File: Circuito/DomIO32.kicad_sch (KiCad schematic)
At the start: 69 parts, among them J1 Conector 1x5, J2 Bornera x2, J3 Bornera x3, J4 Bornera x3, J5 Conn_01x04, J6 Bornera x3, J7 Bornera x2, K1 FINDER-36.11, K2 FINDER-36.11, K3 FINDER-36.11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

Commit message: Componentes actualizados
Regulador 3v3 que soporta Vin de 18V
ESP-02 Version nueva
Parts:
- U1: value LM1117-3.3 -> (none); footprint Package_TO_SOT_SMD:SOT-223-3_TabPin2 -> (none)
- U3: value ESP-02 -> (none); footprint RF_Module:ESP-WROOM-02 -> (none)
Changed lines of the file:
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@@
     (in_bom yes) (on_board yes)
     (property "Reference" "U3" (id 0) (at 180.34 17.3482 0))
-    (property "Value" "ESP-02" (id 1) (at 180.34 19.6596 0))
-    (property "Footprint" "RF_Module:ESP-WROOM-02" (id 2) (at 171.45 50.8 0)
+    (property "Value" "" (id 1) (at 180.34 19.6596 0))
+    (property "Footprint" "" (id 2) (at 171.45 50.8 0)
       (effects (font (size 1.27 1.27) italic) hide)
     )
@@
     (in_bom yes) (on_board yes)
     (property "Reference" "U1" (id 0) (at 77.47 24.3332 0))
-    (property "Value" "LM1117-3.3" (id 1) (at 77.47 26.6446 0))
-    (property "Footprint" "Package_TO_SOT_SMD:SOT-223-3_TabPin2" (id 2) (at 77.47 30.48 0)
+    (property "Value" "" (id 1) (at 77.47 26.6446 0))
+    (property "Footprint" "" (id 2) (at 77.47 30.48 0)
       (effects (font (size 1.27 1.27)) hide)
     )
@@
     )
     (path "/00000000-0000-0000-0000-00005e867b53"
-      (reference "U1") (unit 1) (value "LM1117-3.3") (footprint "Package_TO_SOT_SMD:SOT-223-3_TabPin2")
+      (reference "U1") (unit 1) (value "ZLDO1117QG33TADICT-ND") (footprint "Package_TO_SOT_SMD:SOT-223-3_TabPin2")
     )
     (path "/00000000-0000-0000-0000-0000622ef159"
@@
     )
     (path "/00000000-0000-0000-0000-00005dcb6f71"
-      (reference "U3") (unit 1) (value "ESP-02") (footprint "RF_Module:ESP-WROOM-02")
-    )
-  )
+      (reference "U3") (unit 1) (value "1965-ESP-WROOM-02D-N4CT-ND") (footprint "RF_Module:ESP-WROOM-02")
+    )
+  )

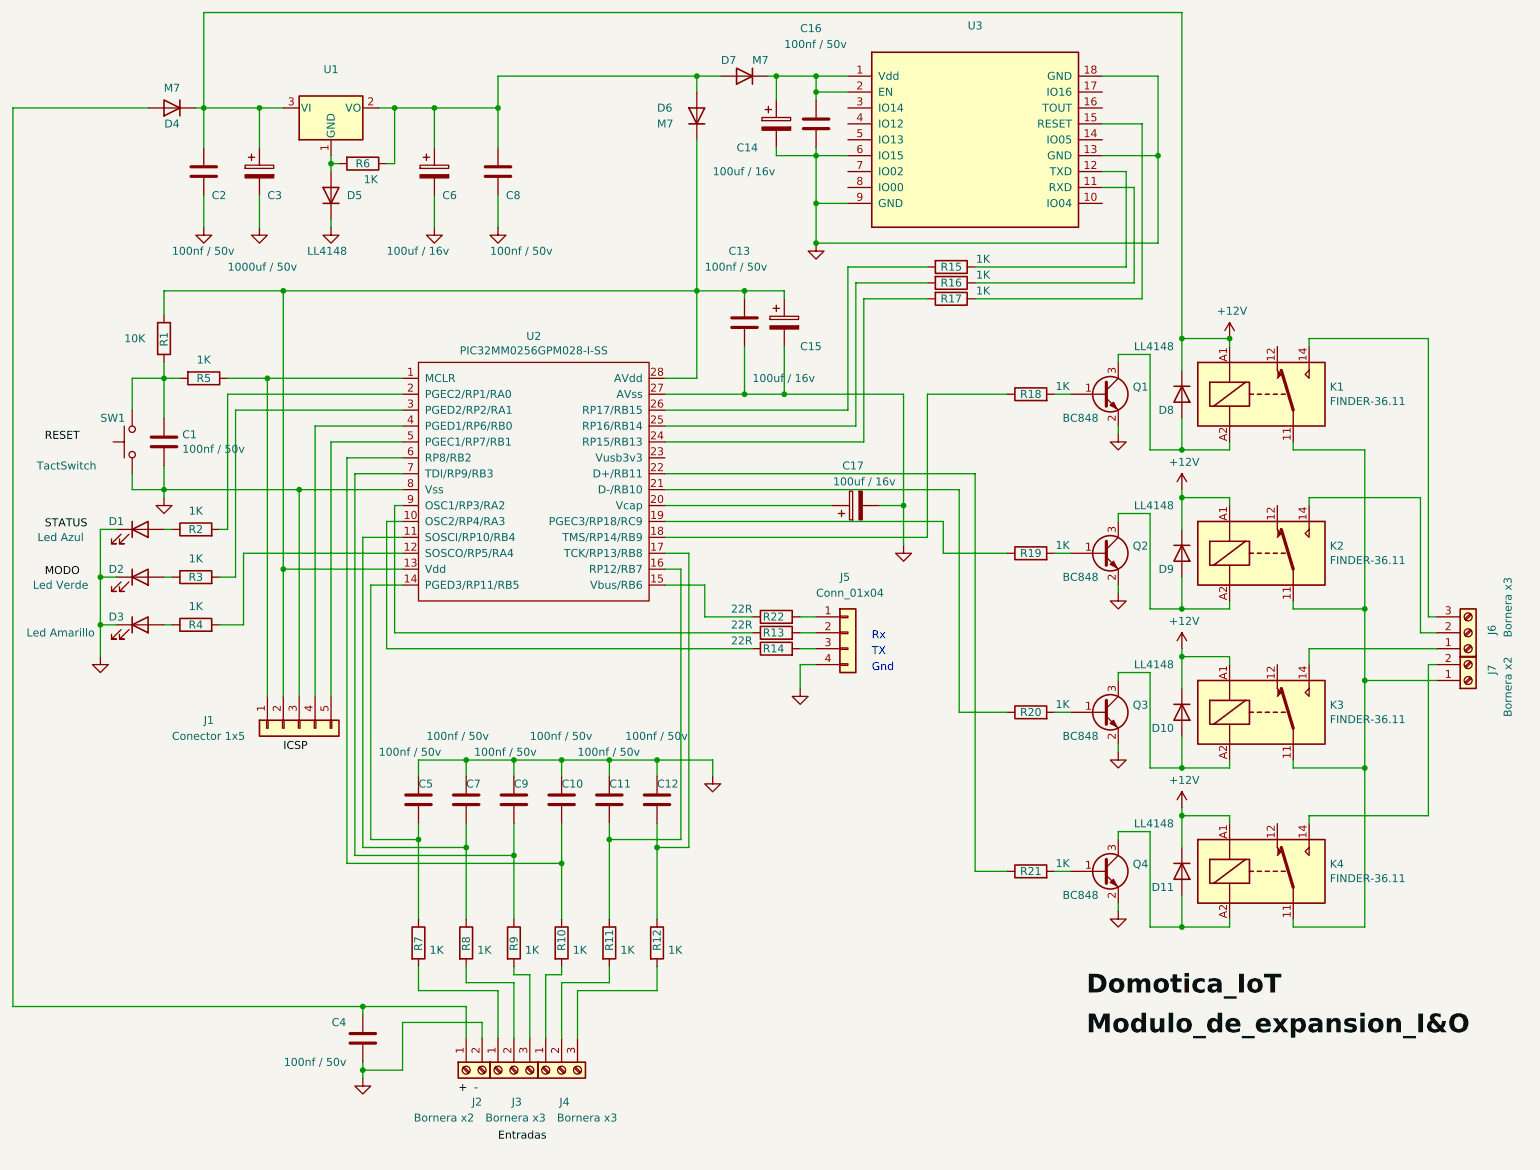
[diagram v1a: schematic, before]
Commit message: Cambio en resistencia 22R por 33R
Cambio en resistencia 22R por 33R
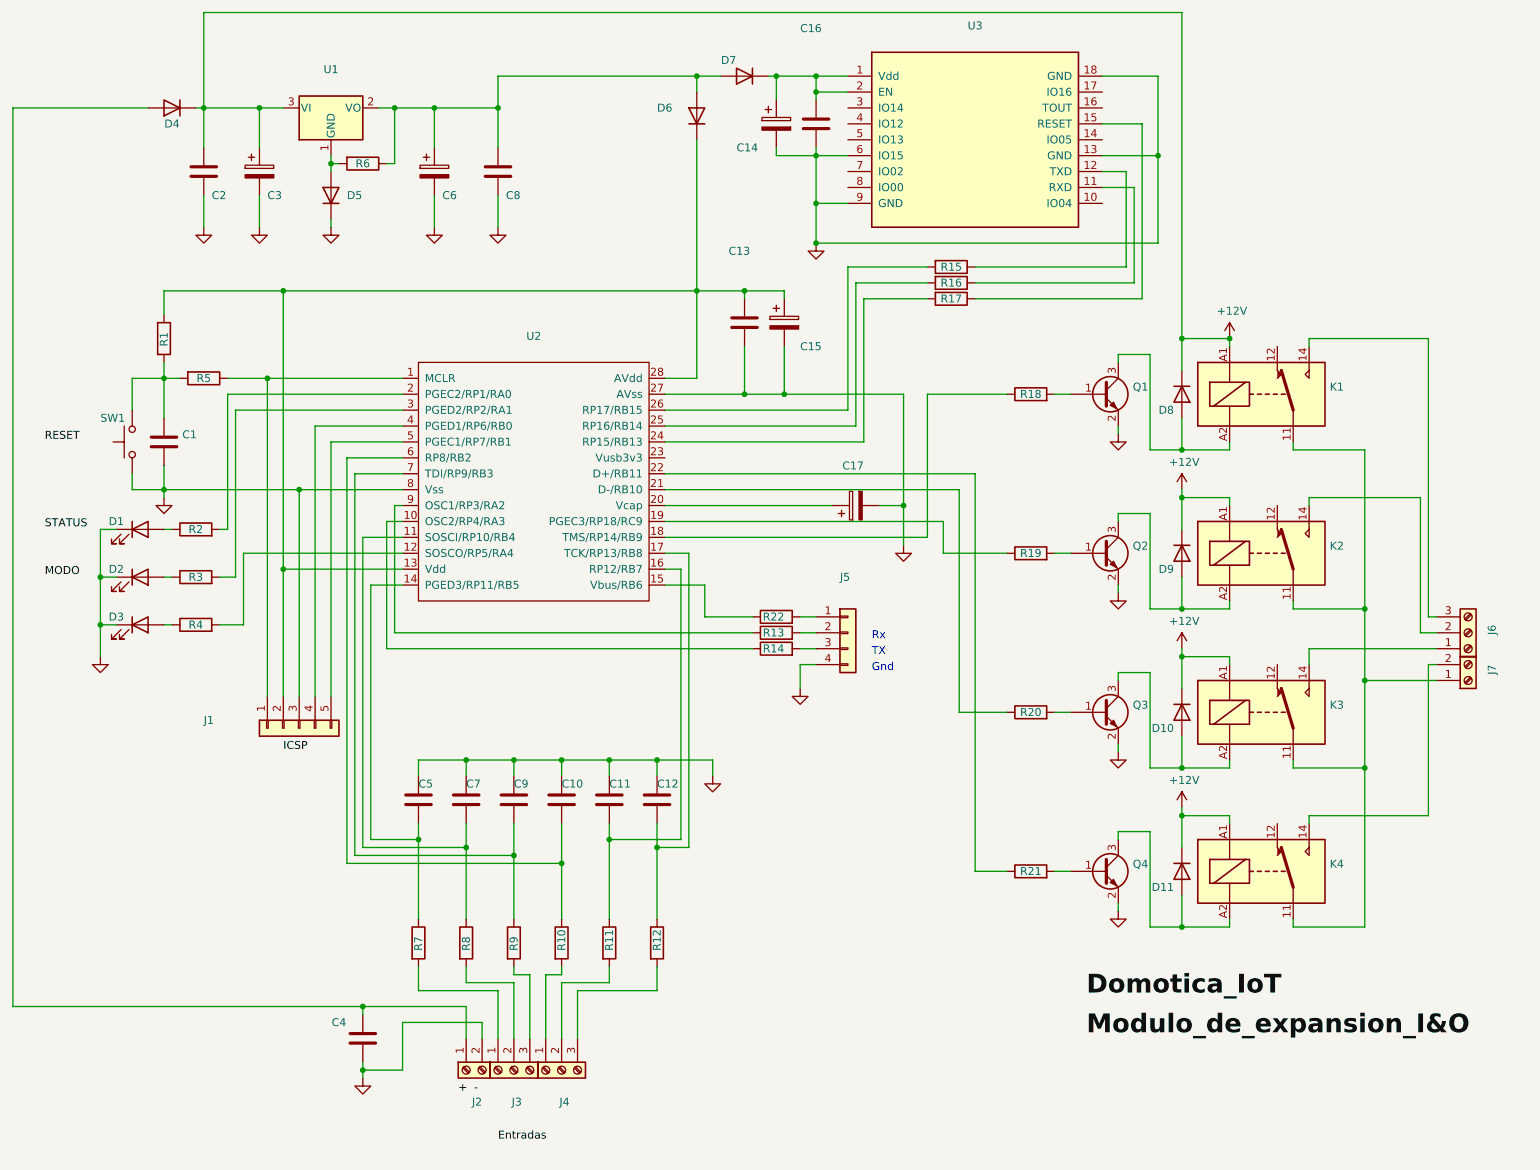
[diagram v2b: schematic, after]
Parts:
- C1, C10, C11, C12, C13, C16, C2, C4, C5, C7, C8, C9: value 100nf / 50v -> (none); footprint Capacitor_SMD:C_0805_2012Metric_Pad1.18x1.45mm_HandSolder -> (none)
- C14, C15, C17, C6: value 100uf / 16v -> (none); footprint Capacitor_THT:CP_Radial_D6.3mm_P2.50mm -> (none)
- C3: value 1000uf / 50v -> (none); footprint Capacitor_THT:CP_Radial_D8.0mm_P5.00mm -> (none)
- D1: value Led Azul -> (none); footprint Diode_SMD:D_0805_2012Metric_Pad1.15x1.40mm_HandSolder -> (none)
- D10, D11, D5, D8, D9: value LL4148 -> (none); footprint Diode_SMD:D_SOD-128 -> (none)
- D2: value Led Verde -> (none); footprint Diode_SMD:D_0805_2012Metric_Pad1.15x1.40mm_HandSolder -> (none)
- D3: value Led Amarillo -> (none); footprint Diode_SMD:D_0805_2012Metric_Pad1.15x1.40mm_HandSolder -> (none)
- D4, D6, D7: value M7 -> (none); footprint Diode_SMD:D_SMA -> (none)
- J1: value Conector 1x5 -> (none); footprint Connector_PinHeader_2.54mm:PinHeader_1x05_P2.54mm_Vertical -> (none)
- J2, J7: value Bornera x2 -> (none); footprint TerminalBlock_Phoenix:TerminalBlock_Phoenix_PT-1,5-2-5.0-H_1x02_P5.00mm_Horizontal -> (none)
- J3, J4, J6: value Bornera x3 -> (none); footprint TerminalBlock_Phoenix:TerminalBlock_Phoenix_PT-1,5-3-5.0-H_1x03_P5.00mm_Horizontal -> (none)
- J5: value Conn_01x04 -> (none); footprint Connector_PinHeader_2.54mm:PinHeader_1x04_P2.54mm_Vertical -> (none)
- K1, K2, K3, K4: value FINDER-36.11 -> (none); footprint Relay_THT:Relay_SPDT_Finder_36.11 -> (none)
- Q1, Q2, Q3, Q4: value BC848 -> (none); footprint Package_TO_SOT_SMD:SOT-23 -> (none)
- R1: value 10K -> (none); footprint Resistor_SMD:R_0805_2012Metric_Pad1.20x1.40mm_HandSolder -> (none)
- R10, R11, R12, R15, R16, R17, R18, R19, R2, R20, R21, R3, R4, R5, R6, R7, R8, R9: value 1K -> (none); footprint Resistor_SMD:R_0805_2012Metric_Pad1.20x1.40mm_HandSolder -> (none)
- R13, R14, R22: value 22R -> (none); footprint Resistor_SMD:R_0805_2012Metric_Pad1.20x1.40mm_HandSolder -> (none)
- SW1: value TactSwitch -> (none); footprint Button_Switch_THT:SW_PUSH_6mm_H5mm -> (none)
- U2: value PIC32MM0256GPM028-I-SS -> (none); footprint Package_SO:SSOP-28_5.3x10.2mm_P0.65mm -> (none)

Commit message: Agregado de MicroSD
Agregado de MicroSD
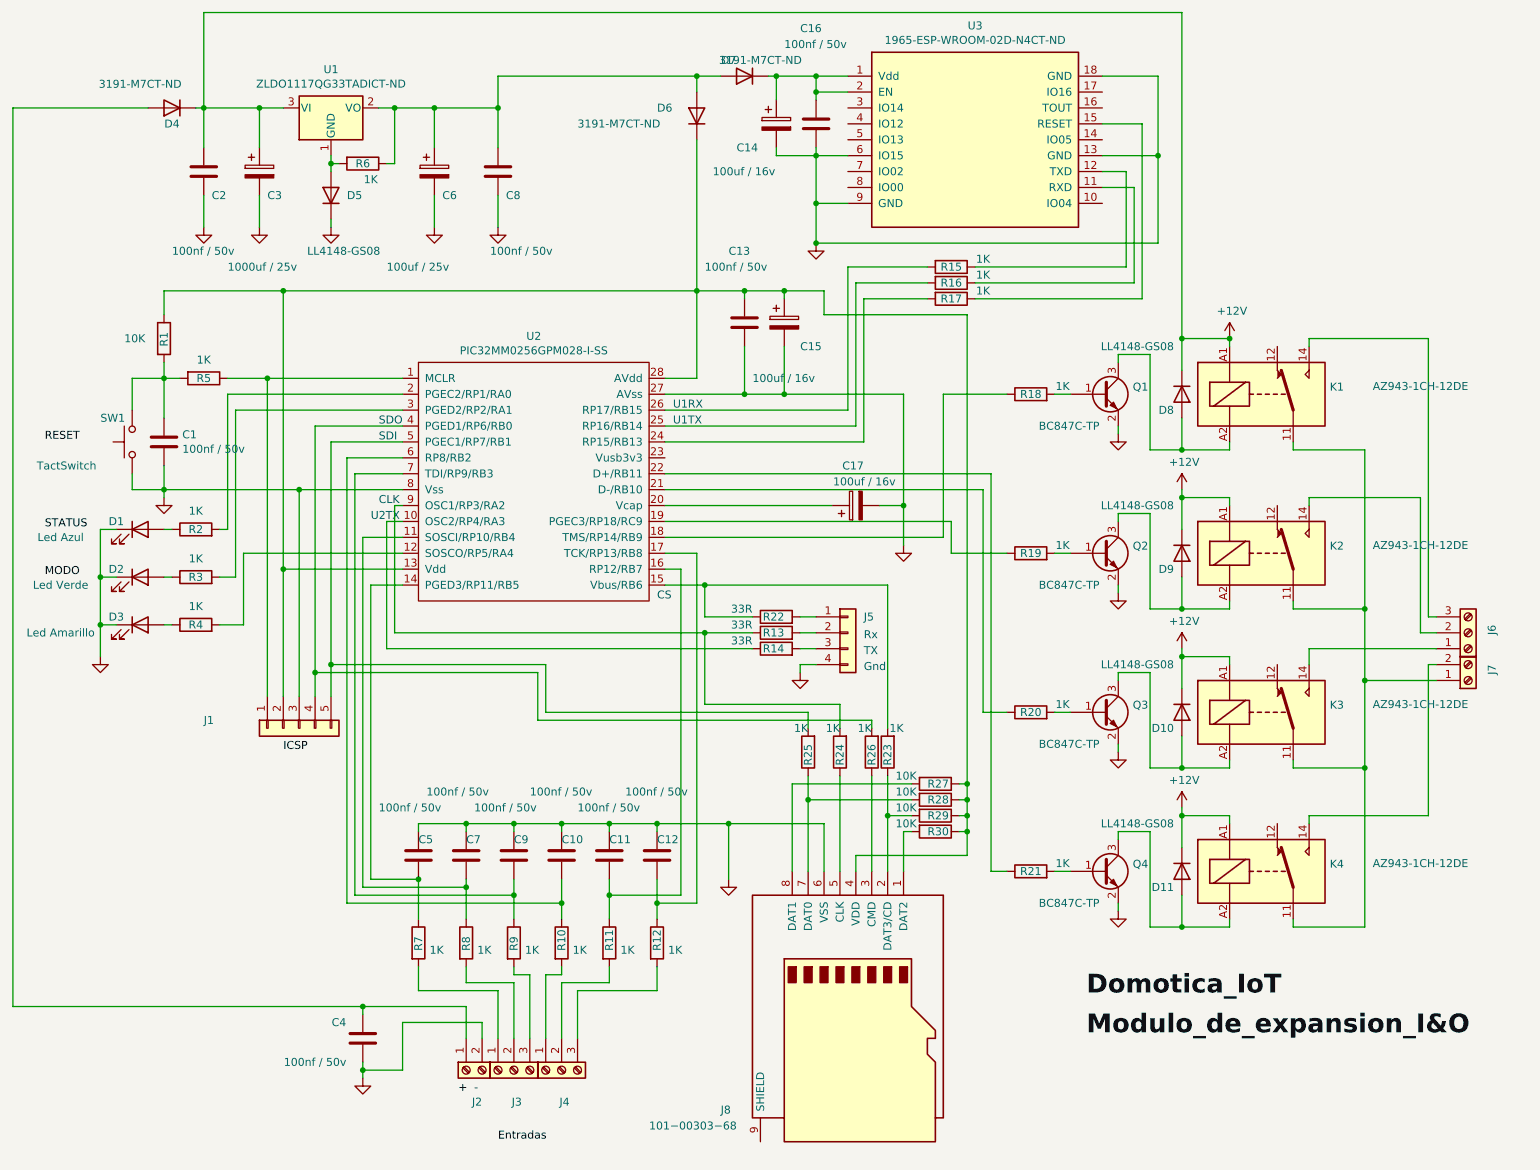
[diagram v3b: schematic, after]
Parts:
- added J8: 101−00303−68, symbol Connector:Micro_SD_Card
- added R23, R24, R25, R26: 1K, Resistor_SMD:R_0805_2012Metric_Pad1.20x1.40mm_HandSolder, symbol Device:R
- added R27, R28, R29, R30: 10K, Resistor_SMD:R_0805_2012Metric_Pad1.20x1.40mm_HandSolder, symbol Device:R
- C1, C10, C11, C12, C13, C16, C2, C4, C5, C7, C8, C9: value (none) -> 100nf / 50v; footprint (none) -> Capacitor_SMD:C_0805_2012Metric_Pad1.18x1.45mm_HandSolder
- C14, C15, C17: value (none) -> 100uf / 16v; footprint (none) -> Capacitor_THT:CP_Radial_D6.3mm_P2.50mm
- C3: value (none) -> 1000uf / 25v; footprint (none) -> Capacitor_THT:CP_Radial_D8.0mm_P5.00mm
- C6: value (none) -> 100uf / 25v; footprint (none) -> Capacitor_THT:CP_Radial_D6.3mm_P2.50mm
- D1: value (none) -> Led Azul; footprint (none) -> Diode_SMD:D_0805_2012Metric_Pad1.15x1.40mm_HandSolder
- D10, D11, D5, D8, D9: value (none) -> LL4148-GS08; footprint (none) -> Diode_SMD:D_SOD-128
- D2: value (none) -> Led Verde; footprint (none) -> Diode_SMD:D_0805_2012Metric_Pad1.15x1.40mm_HandSolder
- D3: value (none) -> Led Amarillo; footprint (none) -> Diode_SMD:D_0805_2012Metric_Pad1.15x1.40mm_HandSolder
- D4, D6, D7: value (none) -> 3191-M7CT-ND; footprint (none) -> Diode_SMD:D_SMA
- J1: value (none) -> Poste; footprint (none) -> Connector_PinHeader_2.54mm:PinHeader_1x05_P2.54mm_Vertical
- J2, J7: value (none) -> 277-1667-ND; footprint (none) -> TerminalBlock_Phoenix:TerminalBlock_Phoenix_PT-1,5-2-5.0-H_1x02_P5.00mm_Horizontal
- J3, J4, J6: value (none) -> 277-1578-ND; footprint (none) -> TerminalBlock_Phoenix:TerminalBlock_Phoenix_PT-1,5-3-5.0-H_1x03_P5.00mm_Horizontal
- J5: value (none) -> Poste; footprint (none) -> Connector_PinHeader_2.54mm:PinHeader_1x04_P2.54mm_Vertical
- K1, K2, K3, K4: value (none) -> AZ943-1CH-12DE; footprint (none) -> Relay_THT:Relay_SPDT_Finder_36.11
- Q1, Q2, Q3, Q4: value (none) -> BC847C-TP; footprint (none) -> Package_TO_SOT_SMD:SOT-23
- R1: value (none) -> 10K; footprint (none) -> Resistor_SMD:R_0805_2012Metric_Pad1.20x1.40mm_HandSolder
- R10, R11, R12, R15, R16, R17, R18, R19, R2, R20, R21, R3, R4, R5, R6, R7, R8, R9: value (none) -> 1K; footprint (none) -> Resistor_SMD:R_0805_2012Metric_Pad1.20x1.40mm_HandSolder
- R13, R14, R22: value (none) -> 33R; footprint (none) -> Resistor_SMD:R_0805_2012Metric_Pad1.20x1.40mm_HandSolder
- SW1: value (none) -> TactSwitch; footprint (none) -> Button_Switch_THT:SW_PUSH_6mm_H5mm
- U1: value (none) -> ZLDO1117QG33TADICT-ND; footprint (none) -> Package_TO_SOT_SMD:SOT-223-3_TabPin2
- U2: value (none) -> PIC32MM0256GPM028-I-SS; footprint (none) -> Package_SO:SSOP-28_5.3x10.2mm_P0.65mm
- U3: value (none) -> 1965-ESP-WROOM-02D-N4CT-ND; footprint (none) -> RF_Module:ESP-WROOM-02
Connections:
- net GND: now also J8.6 (VSS)
- net at C13.1, C15.1, D6.1 (K)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: now also J8.4 (VDD), R27.1, R28.1, R29.1, R30.1
- net at J1.4 (Pin_4), U2.4 (PGED1/RP6/RB0): now also R26.2
- net at J1.5 (Pin_5), U2.5 (PGEC1/RP7/RB1): now also R25.2
- net at R22.1, U2.15 (Vbus/RB6): now also R23.2
- net at R13.1, U2.9 (OSC1/RP3/RA2): now also R24.2
- new net: J8.8 (DAT1), R27.2
- new net: J8.7 (DAT0), R25.1, R28.2
- new net: J8.1 (DAT2), R30.2
- new net: J8.2 (DAT3/CD), R23.1, R29.2
- new net: J8.3 (CMD), R26.1
- new net: J8.5 (CLK), R24.1
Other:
- note added: "CLK"
- note added: "CS"
- note added: "SDI"
- note added: "SDO"
- note added: "U1RX"
- note added: "U1TX"
- note added: "U2TX"
- moved on the sheet: C10, C11, C12, C5, C7, C9

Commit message: MicroSD agregada
MicroSD agregada
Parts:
- removed J5: Poste, Connector_PinHeader_2.54mm:PinHeader_1x04_P2.54mm_Vertical, symbol Connector_Generic:Conn_01x04
- removed R22: 33R, Resistor_SMD:R_0805_2012Metric_Pad1.20x1.40mm_HandSolder, symbol Device:R
- added J5: Poste X 2, Connector_PinHeader_2.54mm:PinHeader_1x02_P2.54mm_Vertical, symbol Connector_Generic:Conn_01x02
- J1: value Poste -> Poste X 5
- J8: value 101−00303−68 -> MEM2067-02-180-00-A; footprint (none) -> Connector_Card:microSD_HC_Wuerth_693072010801
- R13: value 33R -> 0R
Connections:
- net GND: now also J8.9 (SHIELD), J5.2 (Pin_2)
- net at C6.1, C8.1, R6.1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: now also R13.2; no longer D6.2 (A), D7.2 (A)
- net at R24.2, U2.9 (OSC1/RP3/RA2): no longer R13.1
- net at R14.2: now also J5.1 (Pin_1)
- new net: D6.2 (A), D7.2 (A), R13.1
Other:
- note removed: "Rx"
- moved on the sheet: C13, C15, C17, C2, C3, C6, C8, D4, J1, R1, R14, R19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
